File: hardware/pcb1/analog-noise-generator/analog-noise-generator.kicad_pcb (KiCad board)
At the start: 2 copper layers, 12.7 x 53 mm, 81 parts, among them J1 USB_C_Receptacle_USB2.0, J2 Conn_01x03_Pin, J5 Conn_01x04_Pin, J6 Conn_01x04_Pin, J7 Conn_01x02_Pin, J9 Conn_02x04_Odd_Even, U1 STM32F072CBTx, U2 USBLC6-2SC6, U3 LR8321A-T33, U4 LIS2DH12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

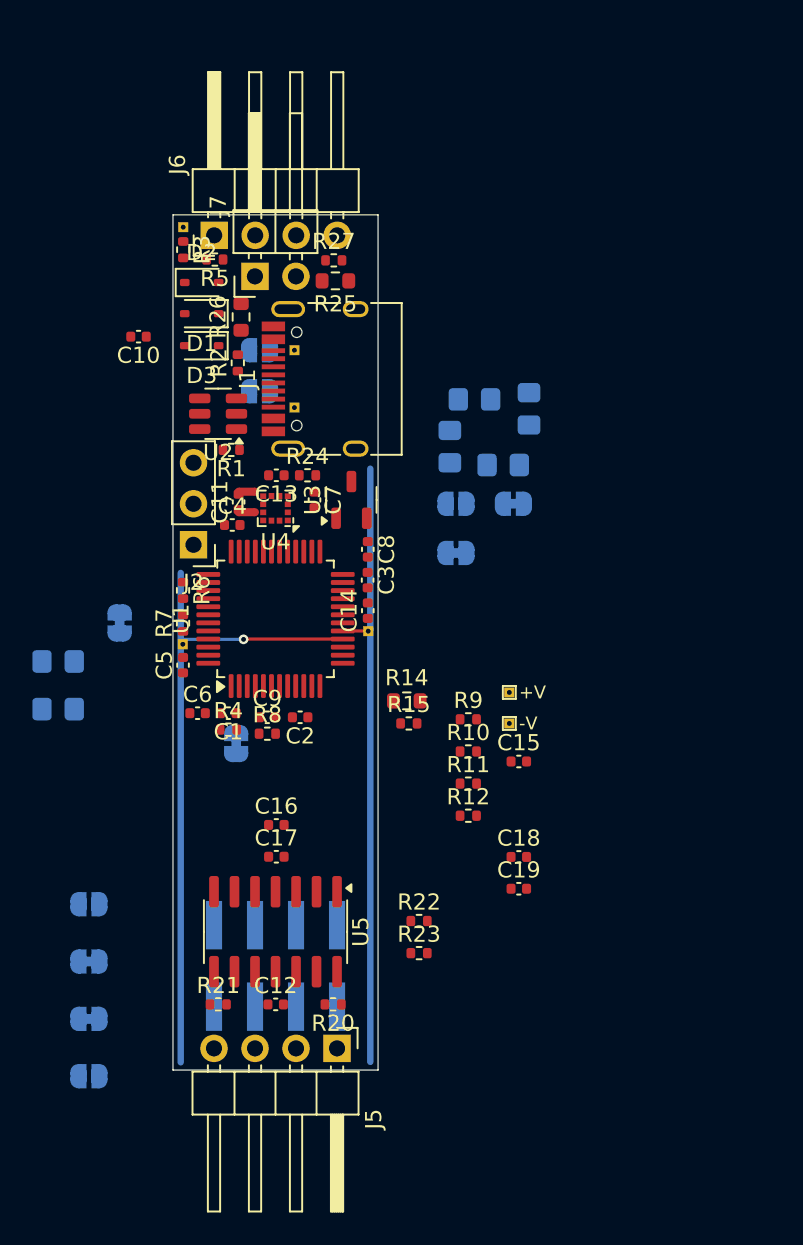
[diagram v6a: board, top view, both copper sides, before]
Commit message: remove negative voltage, add more LCSC part numbers, connect opamps
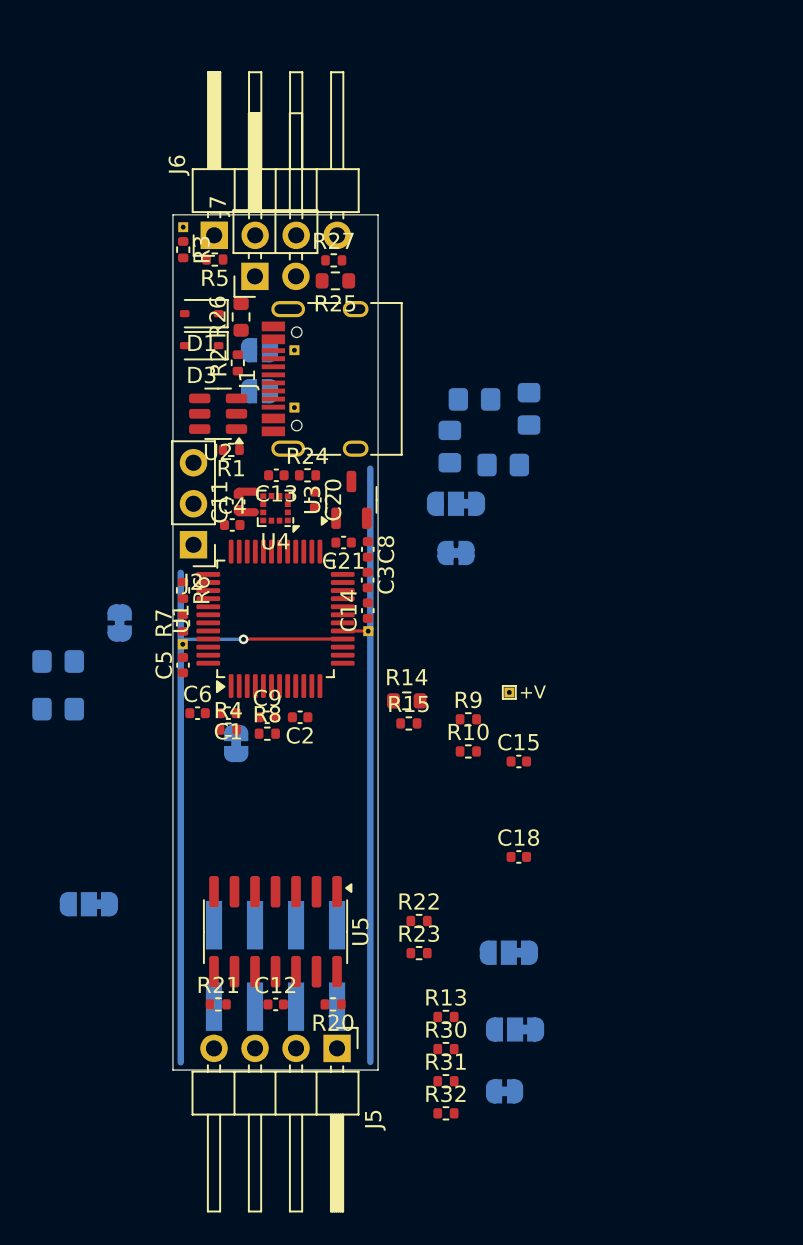
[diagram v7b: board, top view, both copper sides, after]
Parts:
- removed C10, C7: 2u2, 20V, Capacitor_SMD:C_0402_1005Metric
- removed C16, C17: 100n, 50V, Capacitor_SMD:C_0402_1005Metric
- removed C19: 220p, Capacitor_SMD:C_0402_1005Metric
- removed D2: ~, Diode_SMD:D_SOD-323
- removed JP11: SolderJumper_2_Open, Jumper:SolderJumper-2_P1.3mm_Open_RoundedPad1.0x1.5mm
- removed JP9: SolderJumper_2_Bridged, Jumper:SolderJumper-2_P1.3mm_Bridged_RoundedPad1.0x1.5mm
- removed R11: 10k, Resistor_SMD:R_0402_1005Metric
- removed R12: 5.1k, Resistor_SMD:R_0402_1005Metric
- removed TP5: -V, analog-noise-generator:TestPoint_THTPad_small
- added C20: 1u, 25V, Capacitor_SMD:C_0402_1005Metric, F.Cu at (114.2, 74.2)
- added C21: 1u, 25V, Capacitor_SMD:C_0402_1005Metric, F.Cu at (116.0, 76.8)
- added JP12: SolderJumper_2_Bridged, Jumper:SolderJumper-2_P1.3mm_Bridged_RoundedPad1.0x1.5mm, B.Cu at (125.9, 110.8)
- added R13: 10k, Resistor_SMD:R_0402_1005Metric, F.Cu at (122.3, 106.2)
- added R30: 10k, Resistor_SMD:R_0402_1005Metric, F.Cu at (122.3, 108.2)
- added R31: 10k, Resistor_SMD:R_0402_1005Metric, F.Cu at (122.3, 110.2)
- added R32: 10k, Resistor_SMD:R_0402_1005Metric, F.Cu at (122.3, 112.2)
- JP10, JP6: value SolderJumper_2_Bridged -> SolderJumper_3_Bridged12; footprint Jumper:SolderJumper-2_P1.3mm_Bridged_RoundedPad1.0x1.5mm -> Jumper:SolderJumper-3_P1.3mm_Bridged12_RoundedPad1.0x1.5mm
- JP4, JP8: value SolderJumper_2_Open -> SolderJumper_3_Bridged12; footprint Jumper:SolderJumper-2_P1.3mm_Open_RoundedPad1.0x1.5mm -> Jumper:SolderJumper-3_P1.3mm_Bridged12_RoundedPad1.0x1.5mm
- moved JP6 27.8 mm to (126.2, 102.2)
- moved JP10 26.4 mm to (126.6, 107.0)
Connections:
- C12 pad 1: Net-(JP8-A) -> Net-(JP10-C)
- C12 pad 2: Net-(JP10-B) -> Net-(JP12-B)
- JP10 pad 1: -8V -> +8V
- JP10 pad 2: Net-(JP10-B) -> Net-(JP10-C)
- JP4 pad 1: /MISO -> Net-(JP4-A)
- JP4 pad 2: /IMS_SDI -> /OUT1
- JP6 pad 1: /MISO -> Net-(JP6-A)
- JP6 pad 2: /IMS_SDO -> /OUT2
- JP8 pad 1: Net-(JP8-A) -> /IMS_SDO
- JP8 pad 2: +3.3V -> /MISO
- R20 pad 1: Net-(U5A--) -> Net-(R13-Pad2)
- R20 pad 2: /OUT1 -> Net-(JP4-A)
- R21 pad 1: Net-(U5B--) -> Net-(R21-Pad1)
- R21 pad 2: /OUT2 -> Net-(JP6-A)
- U1 pad 12: /V-_sense -> unconnected-(U1-PA2-Pad12)
- U1 pad 2: /PUMP_VNEG -> unconnected-(U1-PC13-Pad2)
- U5 pad 1: Net-(U5A--) -> Net-(R13-Pad2)
- U5 pad 11: Net-(JP10-B) -> Net-(JP12-B)
- U5 pad 4: Net-(JP8-A) -> Net-(JP10-C)
- U5 pad 7: Net-(U5B--) -> Net-(R21-Pad1)

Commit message: start routing
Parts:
- R10: value 10k -> 20k
- TP1, TP2: footprint analog-noise-generator:TestPoint_THTPad_small -> TestPoint:TestPoint_Pad_1.0x1.0mm
- moved JP8 35.7 mm to (128.8, 77.8)
- moved R14 29.1 mm to (107.0, 60.5)
- moved JP4 24.5 mm to (125.8, 98.8)
- moved R15 18.5 mm to (109.7, 72.6)
- moved C18 15.5 mm to (113.3, 88.6), turned to 180 degrees
- moved R27 13.4 mm to (113.5, 72.6)
- moved R24 13.4 mm to (115.1, 59.3)
- moved C15 11.3 mm to (117.5, 83.9), turned to -90 degrees
- moved R28 11.0 mm to (109.2, 85.3), turned to -90 degrees
- moved C14 10.2 mm to (111.6, 72.6), turned to 180 degrees
- moved C13 10.1 mm to (117.5, 81.0), turned to 90 degrees
- moved R29 9.14 mm to (107.2, 85.3), turned to -90 degrees
- moved JP7 5.31 mm to (107.3, 80.8)
- moved R1 4.56 mm to (108.5, 66.5)
- moved JP1 3.94 mm to (107.3, 66.8), turned to 0 degrees
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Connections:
- C13 pad 2: /Vmiddle -> GND
- C14 pad 2: /Vmiddle -> /IMS_GND
- R14 pad 2: /VIN -> /VIN'
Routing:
- net GND: track 0.00 -> 96.0 mm, vias 0 -> 7
- net /VIN_sense: track 0.00 -> 40.6 mm, vias 0 -> 3
- net VBUS: track 0.00 -> 37.2 mm, vias 0 -> 2
- net /IN2L: track 0.00 -> 33.0 mm, vias 0 -> 3
- net +3.3V: track 0.00 -> 32.3 mm, vias 0 -> 4
- net /Vmiddle: track 0.00 -> 30.8 mm, vias 0 -> 2
- net /IN1L: track 0.00 -> 29.0 mm, vias 0 -> 2
- net +8V: track 0.00 -> 26.9 mm, vias 0 -> 3
- net /USB_D-: track 0.00 -> 16.5 mm, vias 0 -> 3
- net /USB_D+: track 0.00 -> 16.2 mm, vias 0 -> 3
- net /SWDIO: track 0.00 -> 15.5 mm
- net /SBU2: track 0.00 -> 11.3 mm, vias 0 -> 1
- net /SWCLK: track 0.00 -> 11.0 mm
- net Net-(J1-CC2): track 0.00 -> 10.2 mm, vias 0 -> 1
- net Net-(J1-CC1): track 0.00 -> 9.95 mm, vias 0 -> 2
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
